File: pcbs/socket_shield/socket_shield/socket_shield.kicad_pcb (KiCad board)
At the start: 2 copper layers, 82.6 x 53.3 mm, 17 parts, among them J1 Power, J2 PWM, J3 Analog, J4 PWM, J5 Analog, J6 Communication, J7 Digital

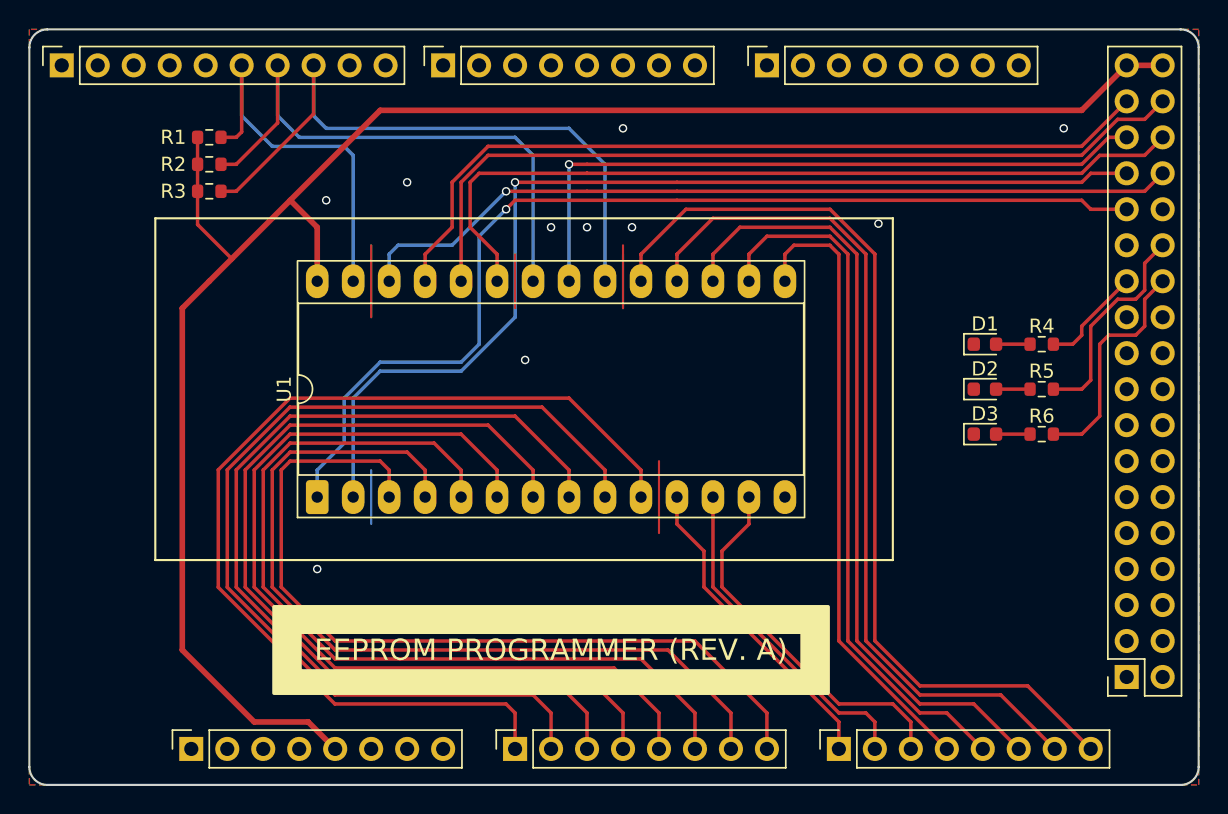
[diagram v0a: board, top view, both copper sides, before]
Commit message: increase hole sizes for socket
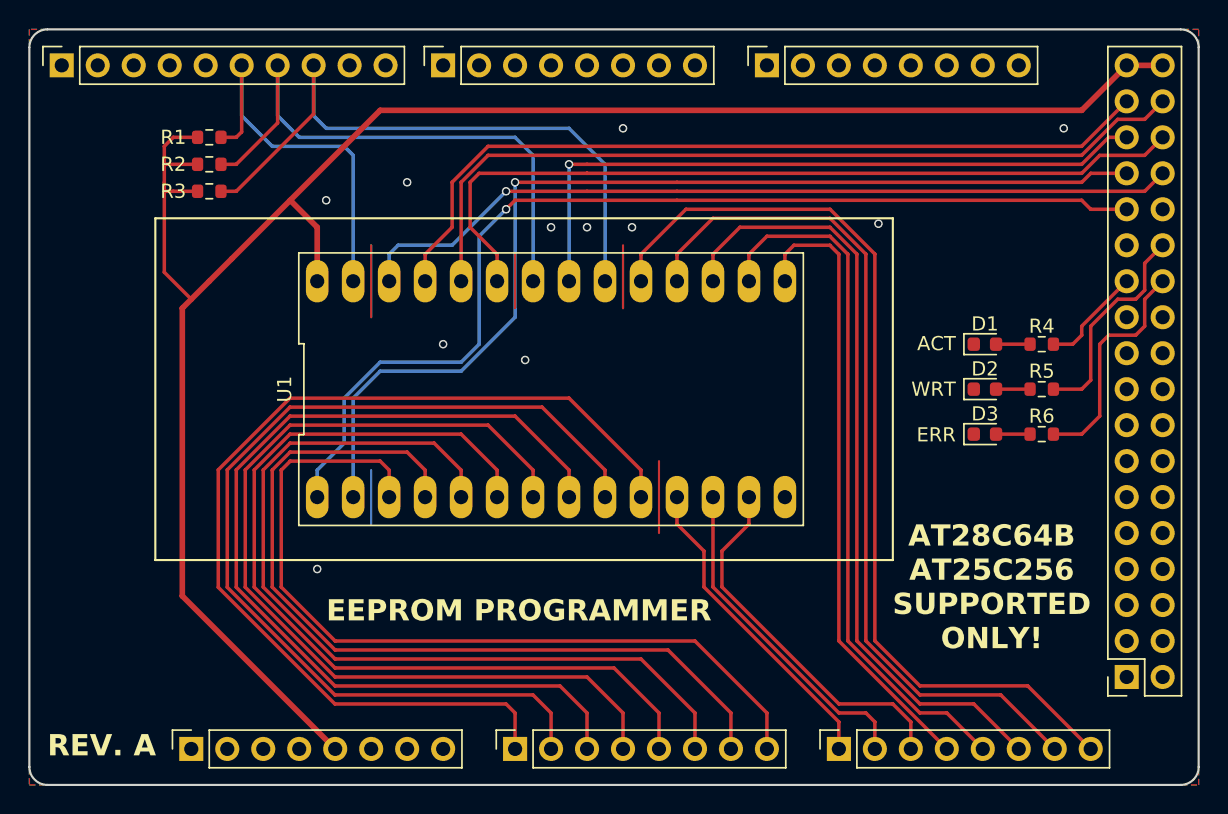
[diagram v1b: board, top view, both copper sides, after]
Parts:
- U1: footprint Package_DIP:DIP-28_W15.24mm_Socket_LongPads -> customs-fp:DIP-28_600_ELL
- moved U1 18.2 mm to (136.8, 72.1), turned to 0 degrees
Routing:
- net +5V: track 130.2 -> 137.3 mm
- net GND: vias 10 -> 11
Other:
- board text added: "ACT WRT ERR"
- board text added: "AT28C64B AT25C256 SUPPORTED ONLY!"
- board text added: "EEPROM PROGRAMMER"
- board text added: "REV. A"
- board text removed: "EEPROM PROGRAMMER (REV. A)"

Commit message: add id pins at designate the socket shield as id 0x01
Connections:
- net /*44 renamed /id5
- net /*45 renamed /id4
- net /*46 renamed /id3
- net /42 renamed /id7
- net /43 renamed /id6
- net /47 renamed /id2
- net /48 renamed /id1
- J7 pad 8: /49 -> GND
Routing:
- net GND: track 0.00 -> 9.94 mm
